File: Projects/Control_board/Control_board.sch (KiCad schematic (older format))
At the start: 50 parts, among them IC1 BD1HD500FVM-CTR, IC2 PCA9615DPJ, J1 5055780871, J2 43045-0200, J3 43045-0200, J4 43045-0200, J5 43045-0401, J6 RJ45, J8 Conn_01x02, K3 PB114024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

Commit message: minor changes
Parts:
- removed D4: LED, LED_SMD:LED_0603_1608Metric, symbol Control_board-rescue:LED-Device
- removed IC1: BD1HD500FVM-CTR, Package_SO:MSOP-8_3x3mm_P0.65mm, symbol Control_board-rescue:BD1HD500FVM-CTR-SamacSys_Parts
- removed R13: 1k, Resistor_SMD:R_0603_1608Metric, symbol Control_board-rescue:R-Device
- C2: footprint Capacitor_SMD:C_0603_1608Metric -> Capacitor_SMD:C_1206_3216Metric
- IC2: footprint SamacSys_Parts:QFN50P300X300X100-10N-D -> Package_SO:TSSOP-10_3x3mm_P0.5mm
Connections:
- net +12V: now also K3.11 (COM), U4.4 (OUT+); no longer U5.4 (OUT+)
- net +5V: now also D3.1 (K), K3.A1 (COIL_1), U5.4 (OUT+)
- net 12V_Fan: now also J2.1, K3.14 (NO)
- net ADJ: now also A1.9 (D6); no longer A1.22 (A3)
- net airstone_pump: now also A1.7 (D4); no longer A1.2 (D0/RX)
- net fan: now also A1.15 (D12), Q4.1, R14.1; no longer A1.1 (D1/TX)
- net pump: now also A1.14 (D11); no longer A1.26 (A7)
- removed net +24V: D3.1 (K), K3.11 (COM), K3.A1 (COIL_1), U4.4 (OUT+)
- net +36V renamed +48V
- removed net mistmaker: A1.25 (A6), Q4.1, R14.1
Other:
- note added: "Remove filter for new LED driver"
- note added: "This circuit is not necesarry"
- note added: "change relay for a 6V or 12 V"
- note added: "pumps"
- note added: "supply for fans"
- moved on the sheet: C2, D3, D5, J2, K3, Q4, R14, R8

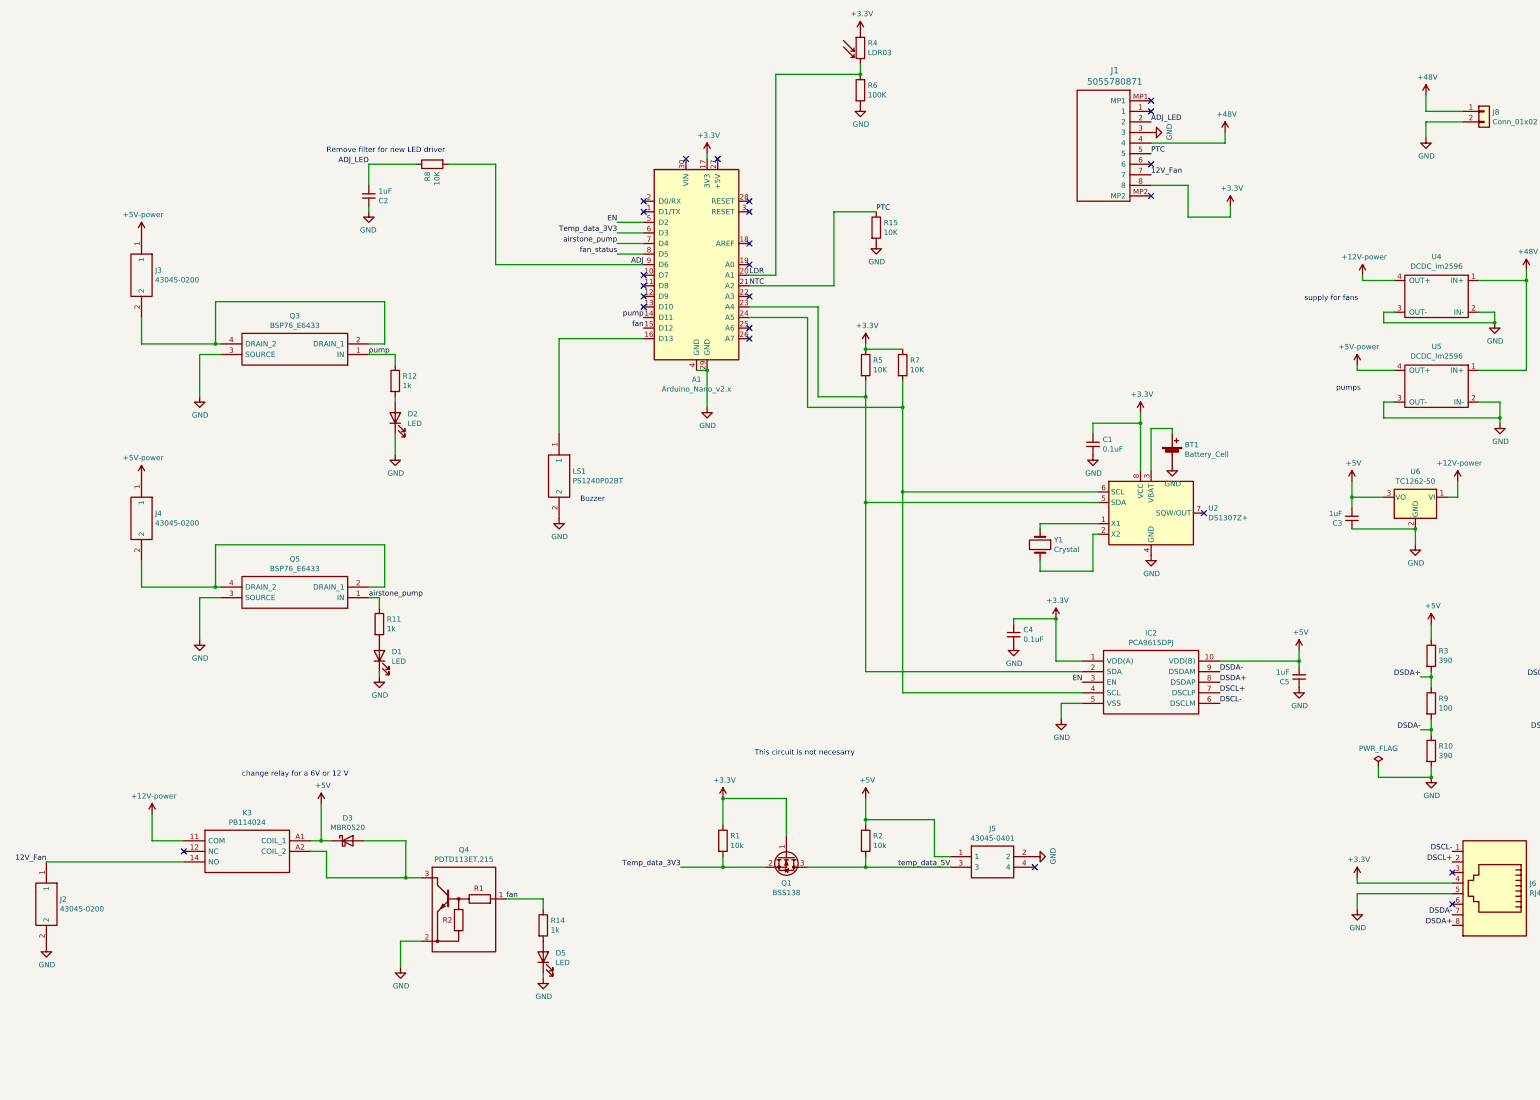
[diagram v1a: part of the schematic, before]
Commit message: new LED board IS3117... plus sorted out libraries
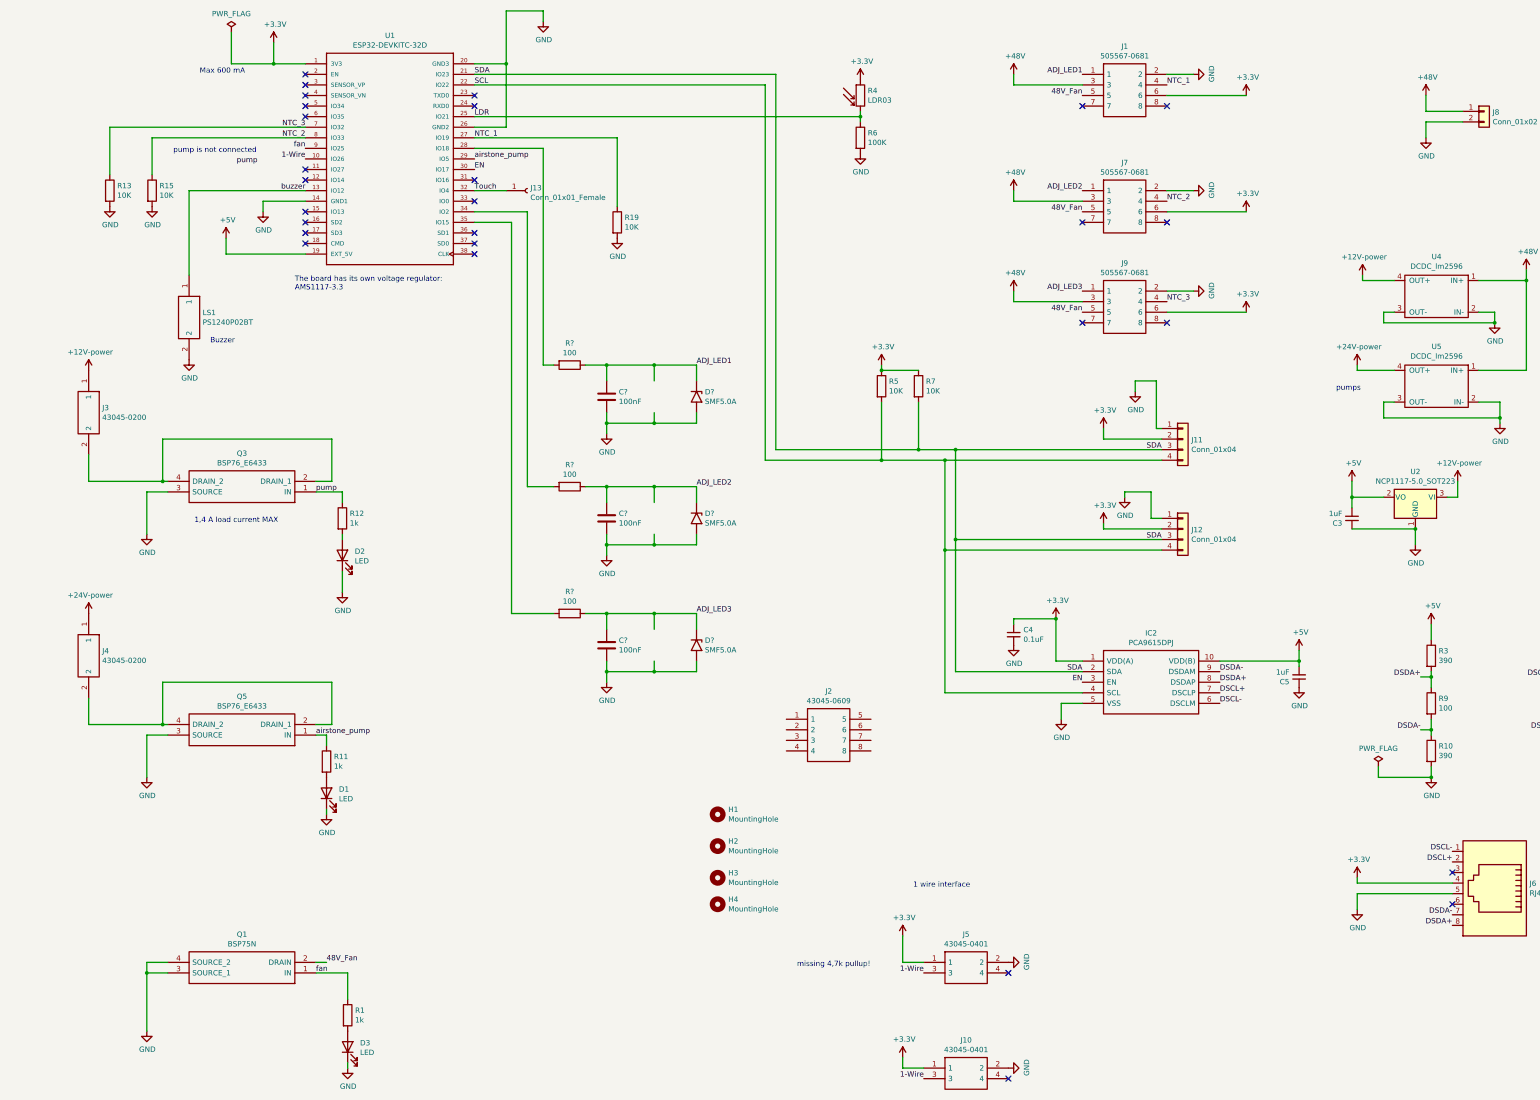
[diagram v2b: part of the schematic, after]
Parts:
- removed A1: Arduino_Nano_v2.x, Module:Arduino_Nano, symbol Control_board-rescue:Arduino_Nano_v2.x-MCU_Module
- removed BT1: Battery_Cell, SamacSys_Parts:BATHLD001, symbol Control_board-rescue:Battery_Cell-Device
- removed C1: 0.1uF, Capacitor_SMD:C_0603_1608Metric, symbol Control_board-rescue:C_Small-Device
- removed C2: 1uF, Capacitor_SMD:C_1206_3216Metric, symbol Control_board-rescue:C_Small-Device
- removed D3: MBR0520, Diode_SMD:D_SOD-123, symbol Control_board-rescue:MBR0520-Diode
- removed D5: LED, LED_SMD:LED_0603_1608Metric, symbol Control_board-rescue:LED-Device
- removed J1: 5055780871, footprints:5055780871, symbol Control_board-rescue:5055780871-My_symbol_library
- removed J2, J3, J4: 43045-0200, Kicad_mylib:Molex_43045-0200, symbol Control_board-rescue:43045-0200-SamacSys_Parts-Control_board-rescue-Control_boa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
- removed K3: PB114024, SamacSys_Parts:PB114024, symbol Control_board-rescue:PB114024-SamacSys_Parts-Control_board-rescue-Control_board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
- removed Q1: BSS138, Package_TO_SOT_SMD:SOT-23, symbol Control_board-rescue:BSS138-Transistor_FET
- removed Q4: PDTD113ET,215, SamacSys_Parts:SOT95P230X110-3N, symbol Control_board-rescue:PDTD113ET,215-SamacSys_Parts-Control_board-rescue-Control_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
- removed R14: 1k, Resistor_SMD:R_0603_1608Metric, symbol Control_board-rescue:R-Device
- removed R2: 10k, Resistor_SMD:R_0603_1608Metric, symbol Control_board-rescue:R-Device
- removed R8: 10K, Resistor_SMD:R_0603_1608Metric, symbol Control_board-rescue:R-Device
- removed U2: DS1307Z+, Package_SO:SOIC-8_3.9x4.9mm_P1.27mm, symbol Control_board-rescue:DS1307Z+-Timer_RTC
- removed U6: TC1262-50, Package_TO_SOT_SMD:SOT-223-3_TabPin2, symbol Control_board-rescue:TC1262-50-Regulator_Linear
- removed Y1: Crystal, SamacSys_Parts:FC135327680KAAG0, symbol Control_board-rescue:Crystal-Device
- added C? (x3): 100nF, symbol Device:C
- added D3: LED, LED_SMD:LED_0603_1608Metric, symbol Control_board-rescue:LED-Device
- added D? (x3): SMF5.0A, Diode_THT:D_DO-201AE_P15.24mm_Horizontal, symbol Diode:1.5KExxA
- added H1, H2, H3, H4: MountingHole, MountingHole:MountingHole_4.3mm_M4, symbol Mechanical:MountingHole
- added J1, J7, J9: 505567-0681, SamacSys_Parts:5055670681, symbol SamacSys_Parts:505567-0681
- added J10: 43045-0401, SamacSys_Parts:430450401, symbol Control_board-rescue:43045-0401-SamacSys_Parts
- added J11, J12: Conn_01x04, Connector_PinHeader_2.54mm:PinHeader_1x04_P2.54mm_Vertical, symbol Connector_Generic:Conn_01x04
- added J13: Conn_01x01_Female, symbol Connector:Conn_01x01_Female
- added J2: 43045-0609, Connector_Molex:Molex_Micro-Fit_3.0_43045-0610_2x03-1MP_P3.00mm_Horizontal, symbol SamacSys_Parts:43045-0609
- added J3, J4: 43045-0200, 43045-0200, symbol SamacSys_Parts:43045-0200
- added Q1: BSP75N, SOT230P700X180-4N, symbol SamacSys_Parts:BSP75N
- added R13, R19: 10K, Resistor_SMD:R_0603_1608Metric, symbol Control_board-rescue:R-Device
- added R? (x3): 100, symbol Device:R
- added U1: ESP32-DEVKITC-32D, ESP32-DEVKITC-32D:MODULE_ESP32-DEVKITC-32D, symbol ESP32-DEVKITC-32D:ESP32-DEVKITC-32D
- added U2: NCP1117-5.0_SOT223, Package_TO_SOT_SMD:SOT-223-3_TabPin2, symbol Regulator_Linear:NCP1117-5.0_SOT223
- R1: value 10k -> 1k
- R4: footprint OptoDevice:R_LDR_10x8.5mm_P7.6mm_Vertical -> LED_SMD:LED_0805_2012Metric
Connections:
- net labels added: +24V-power, 1-Wire, 48V_Fan, ADJ_LED1, ADJ_LED2, ADJ_LED3, NTC_1, NTC_2, NTC_3, SCL, SDA, Touch, buzzer
- net labels removed: +5V-power, 12V_Fan, ADJ, ADJ_LED, NTC, PTC, Temp_data_3V3, fan_status, temp_data_5V
- wire segments 176 -> 215
- no-connect marks 24 -> 28
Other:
- note added: "1 wire interface"
- note added: "1,4 A load current MAX"
- note added: "Max 600 mA"
- note added: "The board has its own voltage regulator: \nAMS1117-3.3"
- note added: "missing 4,7k pullup!"
- note added: "pump is not connected"
- note removed: "Remove filter for new LED driver"
- note removed: "This circuit is not necesarry"
- note removed: "change relay for a 6V or 12 V"
- note removed: "supply for fans"
- moved on the sheet: D1, D2, J5, LS1, Q3, Q5, R11, R12, R15, R4, R5, R6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

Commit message: files after harddrive restore
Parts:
- removed J1, J7, J9: 505567-0681, SamacSys_Parts:5055670681, symbol SamacSys_Parts:505567-0681
- removed J2: 43045-0609, Connector_Molex:Molex_Micro-Fit_3.0_43045-0610_2x03-1MP_P3.00mm_Horizontal, symbol SamacSys_Parts:43045-0609
- removed Q1: BSP75N, SOT230P700X180-4N, symbol SamacSys_Parts:BSP75N
- removed U5: DCDC_lm2596, Kicad_mylib:LM2596_module, symbol Control_board-rescue:DCDC_lm2596-my_library2-Control_board-rescue-Control_board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
- added C7: 100nF, Capacitor_SMD:C_0603_1608Metric, symbol Device:C
- added D4, D5, D6: SMF5.0A, Diode_SMD:D_SOD-123F, symbol Diode:1.5KExxA
- added IC1: VN7050ASTR, SamacSys_Parts:SOIC127P600X175-8N, symbol SamacSys_Parts:VN7050ASTR
- added IC3: PSSI2021SAY,115, SamacSys_Parts:SOT65P210X100-5N, symbol SamacSys_Parts:PSSI2021SAY,115
- added J1, J2, J7: 66200621022, SamacSys_Parts:66200621022, symbol SamacSys_Parts:66200621022
- added Q1: Q_NMOS_GSD, Package_TO_SOT_SMD:SOT-23, symbol Device:Q_NMOS_GSD
- added Q2: BSS138-Transistor_FET, Package_TO_SOT_SMD:SOT-23, symbol Control_board-rescue:BSS138-Transistor_FET
- added R2: 10K, Resistor_SMD:R_0603_1608Metric, symbol Control_board-rescue:R-Device
- added R21: 100, Resistor_SMD:R_0603_1608Metric, symbol Device:R
- added R22: 4.7k, Resistor_SMD:R_0603_1608Metric, symbol Device:R
- added R23: 15k, Resistor_SMD:R_0603_1608Metric, symbol Control_board-rescue:R-Device
- added R24: 39k, Resistor_SMD:R_0603_1608Metric, symbol Device:R
- added R25: 10k, Resistor_SMD:R_0603_1608Metric, symbol Device:R
- added U?: NCP1117-5.0_TO252, Package_TO_SOT_SMD:TO-252-2, symbol Regulator_Linear:NCP1117-5.0_TO252
- C1, C2, C6: renamed from C?; footprint (none) -> Capacitor_SMD:C_0603_1608Metric
- D7, D8, D9: renamed from D?; footprint Diode_THT:D_DO-201AE_P15.24mm_Horizontal -> Diode_SMD:D_SOD-123F
- J13: footprint (none) -> Connector_PinHeader_1.00mm:PinHeader_1x01_P1.00mm_Horizontal
- J3, J4: footprint 43045-0200 -> footprints:43045-0200
- R14, R20, R8: renamed from R?; footprint (none) -> Resistor_SMD:R_0603_1608Metric
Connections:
- net labels added: 12V_Fan
- net labels removed: +24V-power, 48V_Fan
- wire segments 215 -> 244
- no-connect marks 28 -> 22
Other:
- note added: "1.8 A"
- note added: "700 mA"
- note added: "Protection circuit for 1-wire interface:\nhttps://www.maximintegrated.com/en/design/technical-documents/tutorials/5/5026.html"
- note added: "need heatsink/groundstitching"
- note added: "obsolete?"
- note removed: "missing 4,7k pullup!"
- note removed: "pump is not connected"
- note removed: "pumps"
- moved on the sheet: D3, D7, H1, H2, H3, H4, J10, J5, LS1, R1, R13, R15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
